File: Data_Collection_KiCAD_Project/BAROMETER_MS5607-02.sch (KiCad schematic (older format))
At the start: 2 parts

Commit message: Fixed Component Libraries
Changed over from project specific to global libraries.
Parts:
- C?: symbol Data_Collection_KiCAD_Project-rescue:C-Device -> Data_Collection_KiCAD_Project-rescue:C-Device-Data_Collection_KiCAD_Project-rescue
- U?: symbol Data_Collection_KiCAD_Project-rescue:MS5607-02BA-Sensor_Pressure -> Data_Collection_KiCAD_Project-rescue:MS5607-02BA-Sensor_Pressure-Data_Collection_KiCAD_Project-rescue
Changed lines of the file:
@@
 $Descr A4 11693 8268
 encoding utf-8
-Sheet 7 10
+Sheet 7 9
 Title "MS5607-02BA Barometer Chip"
 Date "2021-10-01"
@@
 $EndDescr
 $Comp
-L Data_Collection_KiCAD_Project-rescue:MS5607-02BA-Sensor_Pressure U?
+L Data_Collection_KiCAD_Project-rescue:MS5607-02BA-Sensor_Pressure-Data_Collection_KiCAD_Project-rescue U?
 U 1 1 6161026E
 P 5900 3650
@@
 $EndComp
 $Comp
-L Data_Collection_KiCAD_Project-rescue:+3.3V-power #PWR?
+L Data_Collection_KiCAD_Project-rescue:+3.3V-power-Data_Collection_KiCAD_Project-rescue #PWR?
 U 1 1 61610274
 P 6350 3150
@@
 	5900 3200 5900 3250
 $Comp
-L Data_Collection_KiCAD_Project-rescue:GND-power #PWR?
+L Data_Collection_KiCAD_Project-rescue:GND-power-Data_Collection_KiCAD_Project-rescue #PWR?
 U 1 1 6161027B
 P 5900 4150
@@
 	5900 4050 5900 4100
 $Comp
-L Data_Collection_KiCAD_Project-rescue:C-Device C?
+L Data_Collection_KiCAD_Project-rescue:C-Device-Data_Collection_KiCAD_Project-rescue C?
 U 1 1 61610282
 P 6350 3650

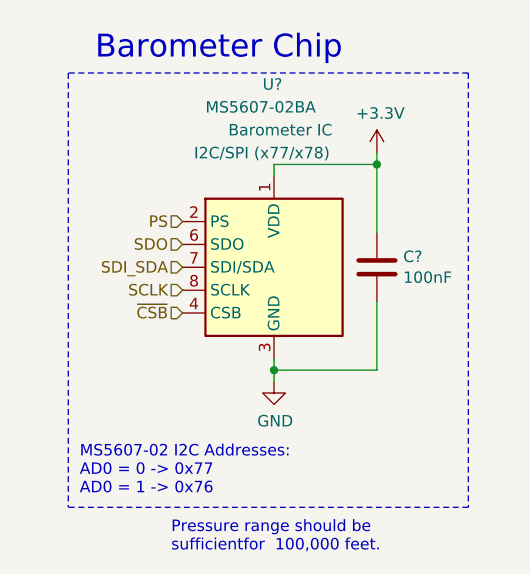
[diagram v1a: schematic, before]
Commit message: footprint and value changes
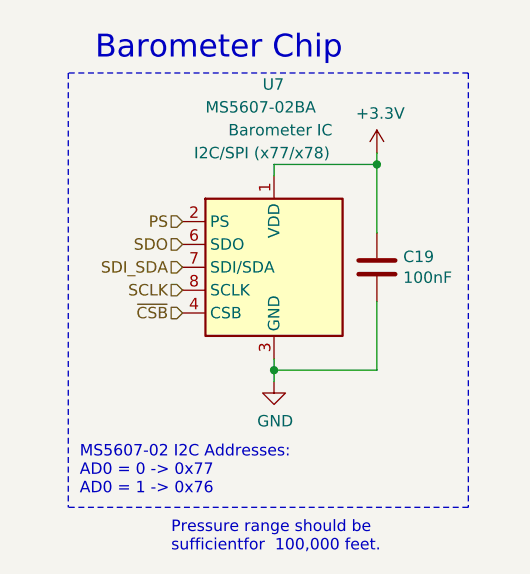
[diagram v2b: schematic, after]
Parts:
- C19: renamed from C?; footprint (none) -> Capacitor_SMD:C_0603_1608Metric
- gave numbers to parts that had none: 1
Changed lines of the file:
@@
 P 5900 3650
 AR Path="/6161026E" Ref="U?"  Part="1"
-AR Path="/615B3F6F/6161026E" Ref="U?"  Part="1"
-F 0 "U?" H 5850 4450 50  0000 L CNN
+AR Path="/615B3F6F/6161026E" Ref="U7"  Part="1"
+F 0 "U7" H 5850 4450 50  0000 L CNN
 F 1 "MS5607-02BA" H 5600 4350 50  0000 L CNN
 F 2 "Package_LGA:LGA-8_3x5mm_P1.25mm" H 5900 3650 50  0001 C CNN
@@
 P 6350 3150
 AR Path="/61610274" Ref="#PWR?"  Part="1"
-AR Path="/615B3F6F/61610274" Ref="#PWR?"  Part="1"
-F 0 "#PWR?" H 6350 3000 50  0001 C CNN
+AR Path="/615B3F6F/61610274" Ref="#PWR047"  Part="1"
+F 0 "#PWR047" H 6350 3000 50  0001 C CNN
 F 1 "+3.3V" H 6365 3323 50  0000 C CNN
 F 2 "" H 6350 3150 50  0001 C CNN
@@
 P 5900 4150
 AR Path="/6161027B" Ref="#PWR?"  Part="1"
-AR Path="/615B3F6F/6161027B" Ref="#PWR?"  Part="1"
-F 0 "#PWR?" H 5900 3900 50  0001 C CNN
+AR Path="/615B3F6F/6161027B" Ref="#PWR046"  Part="1"
+F 0 "#PWR046" H 5900 3900 50  0001 C CNN
 F 1 "GND" H 5905 3977 50  0000 C CNN
 F 2 "" H 5900 4150 50  0001 C CNN
@@
 P 6350 3650
 AR Path="/61610282" Ref="C?"  Part="1"
-AR Path="/615B3F6F/61610282" Ref="C?"  Part="1"
-F 0 "C?" H 6465 3696 50  0000 L CNN
+AR Path="/615B3F6F/61610282" Ref="C19"  Part="1"
+F 0 "C19" H 6465 3696 50  0000 L CNN
 F 1 "100nF" H 6465 3605 50  0000 L CNN
-F 2 "" H 6388 3500 50  0001 C CNN
+F 2 "Capacitor_SMD:C_0603_1608Metric" H 6388 3500 50  0001 C CNN
 F 3 "~" H 6350 3650 50  0001 C CNN
 	1    6350 3650

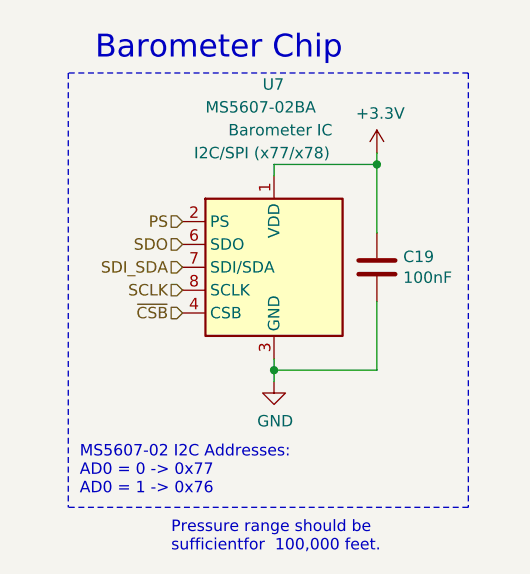
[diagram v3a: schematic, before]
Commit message: footprint changes
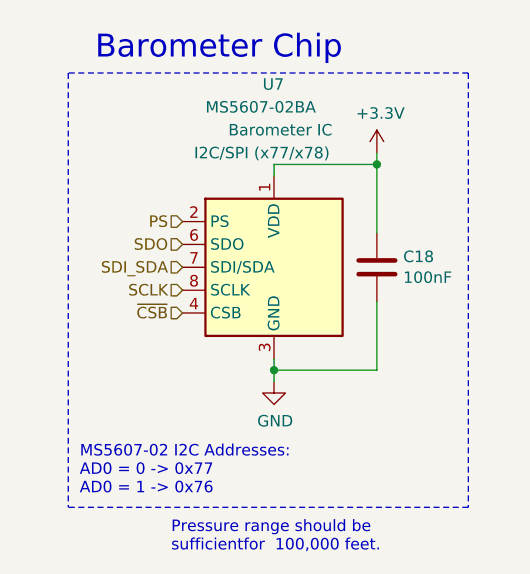
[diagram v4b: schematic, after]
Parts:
- renumbered C19 to C18
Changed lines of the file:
@@
 P 6350 3150
 AR Path="/61610274" Ref="#PWR?"  Part="1"
-AR Path="/615B3F6F/61610274" Ref="#PWR047"  Part="1"
-F 0 "#PWR047" H 6350 3000 50  0001 C CNN
+AR Path="/615B3F6F/61610274" Ref="#PWR040"  Part="1"
+F 0 "#PWR040" H 6350 3000 50  0001 C CNN
 F 1 "+3.3V" H 6365 3323 50  0000 C CNN
 F 2 "" H 6350 3150 50  0001 C CNN
@@
 P 5900 4150
 AR Path="/6161027B" Ref="#PWR?"  Part="1"
-AR Path="/615B3F6F/6161027B" Ref="#PWR046"  Part="1"
-F 0 "#PWR046" H 5900 3900 50  0001 C CNN
+AR Path="/615B3F6F/6161027B" Ref="#PWR039"  Part="1"
+F 0 "#PWR039" H 5900 3900 50  0001 C CNN
 F 1 "GND" H 5905 3977 50  0000 C CNN
 F 2 "" H 5900 4150 50  0001 C CNN
@@
 P 6350 3650
 AR Path="/61610282" Ref="C?"  Part="1"
-AR Path="/615B3F6F/61610282" Ref="C19"  Part="1"
-F 0 "C19" H 6465 3696 50  0000 L CNN
+AR Path="/615B3F6F/61610282" Ref="C18"  Part="1"
+F 0 "C18" H 6465 3696 50  0000 L CNN
 F 1 "100nF" H 6465 3605 50  0000 L CNN
 F 2 "Capacitor_SMD:C_0603_1608Metric" H 6388 3500 50  0001 C CNN
